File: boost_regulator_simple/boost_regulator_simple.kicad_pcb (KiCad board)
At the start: 2 copper layers, 62.2 x 50.8 mm, 18 parts, among them Q1 MOS_N, U1 LM555N

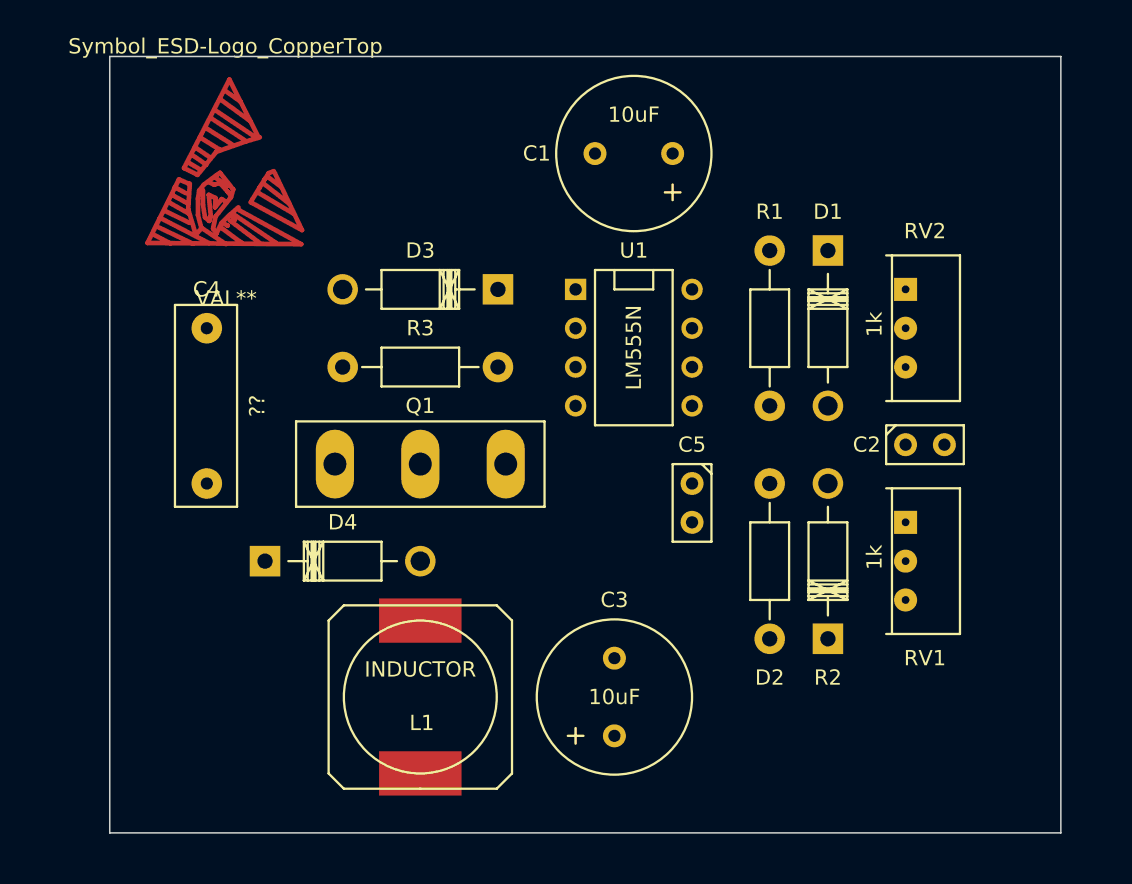
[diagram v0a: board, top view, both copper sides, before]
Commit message: [boost_regulator_simple] First pass layout complete.
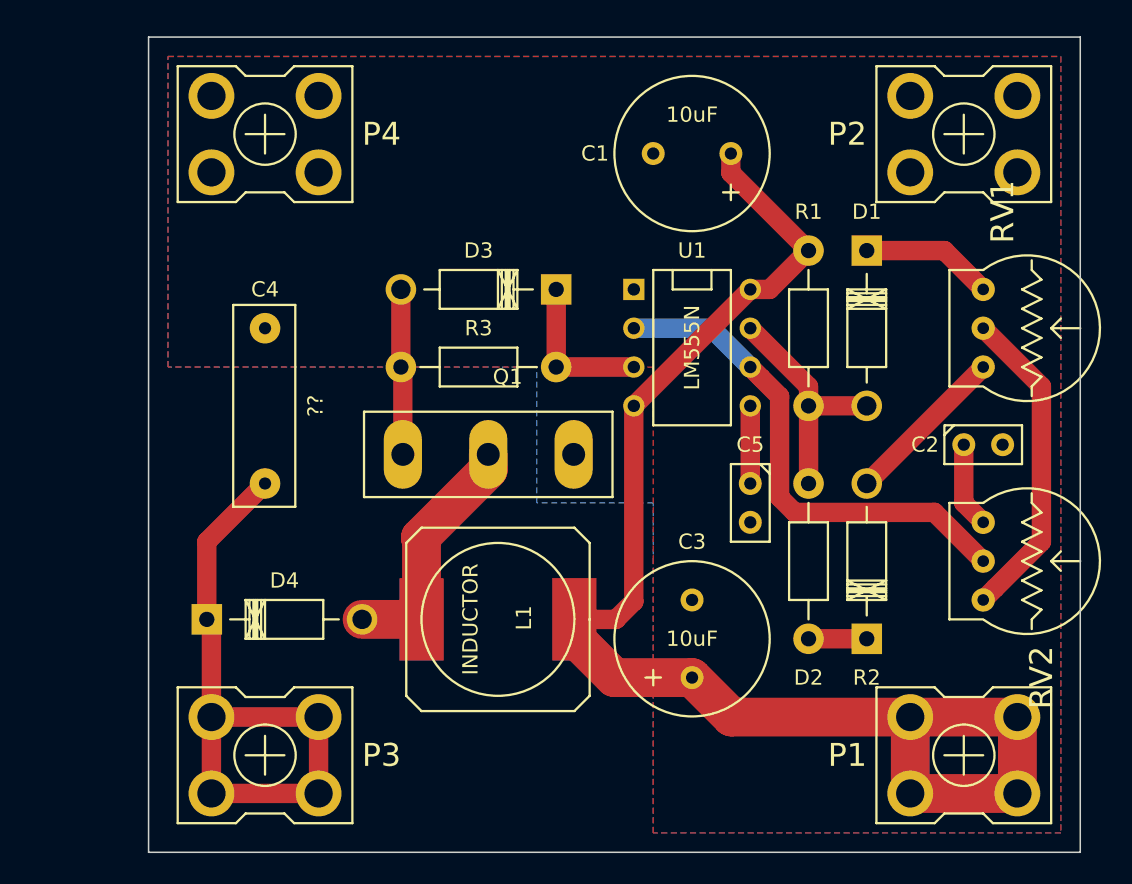
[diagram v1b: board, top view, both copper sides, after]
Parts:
- removed Symbol_ESD-Logo_CopperTop: VAL**, Symbols:Symbol_ESD-Logo_CopperTop
- added P1: CONN_01X01, NQBit:Screw_Terminal_x1, F.Cu at (133.3, 99.1)
- added P2: CONN_01X01, NQBit:Screw_Terminal_x1, F.Cu at (133.3, 58.4)
- added P3: CONN_01X01, NQBit:Screw_Terminal_x1, F.Cu at (87.6, 99.1)
- added P4: CONN_01X01, NQBit:Screw_Terminal_x1, F.Cu at (87.6, 58.4)
- Q1: value MOS_N -> MOSFET-N
- RV1, RV2: footprint Potentiometers:Potentiometer_Trimmer-Suntan-TSR-3386C -> NQBit:Potentiometer_Thumbwheel
- moved RV2 18.5 mm to (134.6, 86.4), turned to 90 degrees
- moved RV1 13.7 mm to (134.6, 71.1), turned to 90 degrees
- moved L1 7.18 mm to (102.9, 90.2), turned to 180 degrees
- moved C3 6.35 mm to (115.6, 94.0)
- moved D4 5.39 mm to (88.9, 90.2)
- moved Q1 4.49 mm to (102.2, 79.4)
- moved C1 3.81 mm to (118.1, 59.7)
- moved C2 3.81 mm to (134.6, 78.7)
- moved C4 3.81 mm to (87.6, 76.2)
- moved C5 3.81 mm to (119.4, 82.5)
- moved D3 3.81 mm to (101.6, 68.6)
- moved R3 3.81 mm to (101.6, 73.7)
- moved U1 3.81 mm to (115.6, 72.4)
- moved D1 2.54 mm to (127.0, 71.1)
- moved D2 2.54 mm to (127.0, 86.4)
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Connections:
- net Net-(C4-Pad1) renamed /BOOST_OUT
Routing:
- net VCC: track 0.00 -> 90.6 mm
- net /BOOST_OUT: track 0.00 -> 41.0 mm
- net Net-(RV2-Pad2): track 0.00 -> 33.0 mm
- net Net-(RV1-Pad2): track 0.00 -> 20.9 mm
- net Net-(D4-Pad1): track 0.00 -> 16.6 mm
- net Net-(D1-Pad1): track 0.00 -> 15.5 mm
- net Net-(D3-Pad1): track 0.00 -> 10.8 mm
- net Net-(D2-Pad1): track 0.00 -> 10.8 mm
- net Net-(D3-Pad2): track 0.00 -> 10.2 mm
- net Net-(D1-Pad2): track 0.00 -> 8.67 mm
- net Net-(C2-Pad1): track 0.00 -> 5.61 mm
- net Net-(C5-Pad1): track 0.00 -> 5.08 mm
- net Net-(D2-Pad2): track 0.00 -> 3.81 mm
- added copper zone on B.Cu, net GND
- added copper zone on F.Cu, net GND
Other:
- board size 62.2 x 50.8 mm -> 61 x 53.3 mm

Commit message: [boost_regulator_simple] Made changes to reduce EMI and other cosmetics.
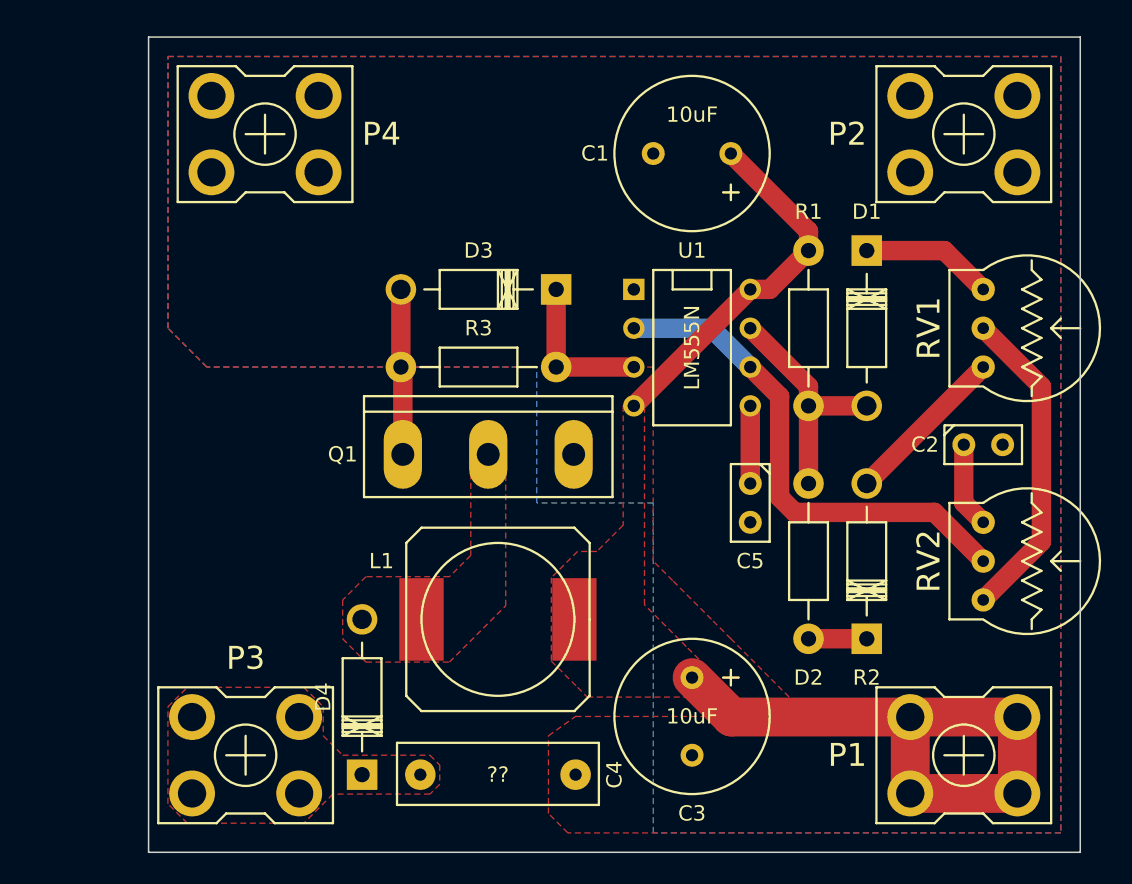
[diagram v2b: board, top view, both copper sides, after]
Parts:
- Q1: footprint Transistors_TO-247:TO-247_Vertical_Neutral123 -> NQBit:TO-247_Vertical_Neutral123
- moved C4 28.5 mm to (102.9, 100.3), turned to 0 degrees
- moved D4 7.18 mm to (94.0, 95.2), turned to 270 degrees
- moved P3 1.27 mm to (86.4, 99.1)
- turned C3 to 270 degrees
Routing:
- net /BOOST_OUT: track 41.0 -> 0.00 mm
- net VCC: track 90.6 -> 63.5 mm
- net Net-(D4-Pad1): track 16.6 -> 0.00 mm
- added copper zone on F.Cu, net /BOOST_OUT
- added copper zone on F.Cu, net Net-(D4-Pad1)
- added copper zone on F.Cu, net VCC
